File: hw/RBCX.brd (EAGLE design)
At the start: 100 x 100 mm, 463 parts, among them IC1 AMS1117-3.3, IC10 INA180A4, IC11 INA180A4, IC12 MPU-6050, IC13 STM32F103VCT6, IC2 DRV8833PWP, IC3 INA180A4, IC4 INA180A4, IC5 DRV8833PWP, IC6 INA180A4, IC7 INA180A4, IC8 INA180A4, IC9 INA180A4, P1 M1, P2 M2, P3 M3, P4 M4, Q1 NCE20P45Q, Q10 2N7002, Q2 NCE20P45Q, Q3 2N7002, Q4 2N7002, Q5 2N7002, Q6 2N7002, Q7 2N7002, Q8 2N7002, Q9 2N7002, X1 POWER_IN, X2 POWER_OUT, X3 52559-3092, X4 uUSB, Y1 5032/2P, Y2 3215_2P

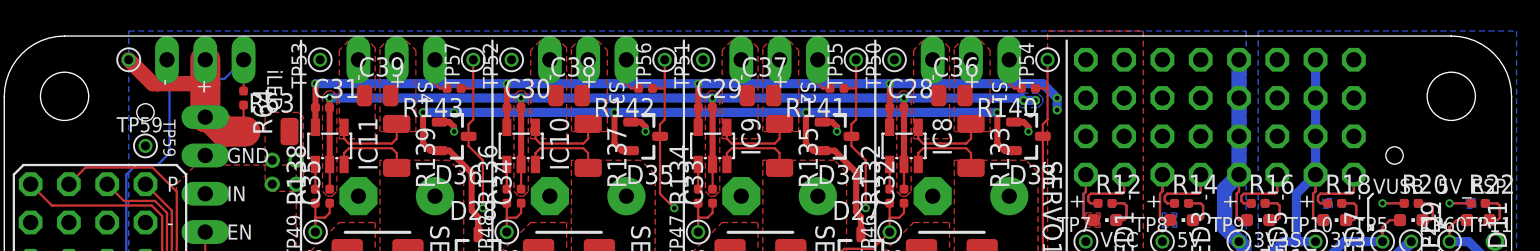
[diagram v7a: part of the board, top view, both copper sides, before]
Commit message: hw: add two small areas of unmasked GND plane for oscilloscope clip
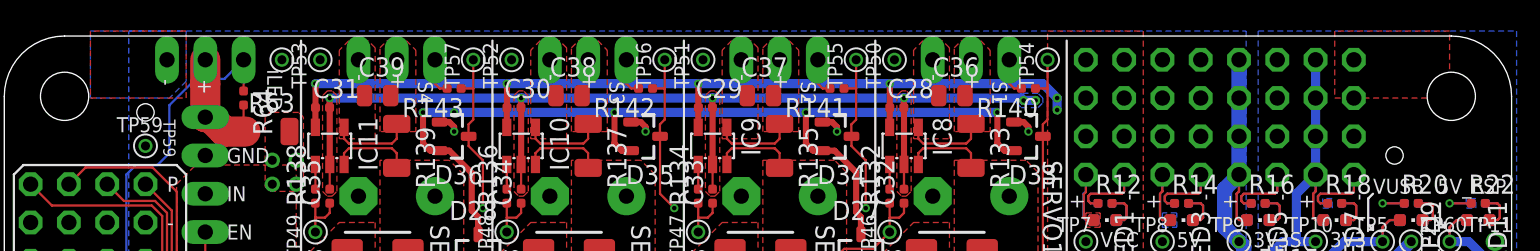
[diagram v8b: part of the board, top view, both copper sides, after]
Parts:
- moved TP15 10.2 mm to (18.4, 98.4)
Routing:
- net ILED-5V: track 98.2 -> 97.4 mm
- net ILED_PWR: track 14.4 -> 15.1 mm
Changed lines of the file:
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@@
 <layer number="13" name="Route13" color="21" fill="1" visible="no" active="no"/>
 <layer number="14" name="Route14" color="22" fill="1" visible="no" active="no"/>
-<layer number="15" name="Layer3-GND" color="23" fill="1" visible="yes" active="yes"/>
+<layer number="15" name="Layer3-GND" color="23" fill="1" visible="no" active="yes"/>
 <layer number="16" name="Bottom" color="1" fill="1" visible="yes" active="yes"/>
 <layer number="17" name="Pads" color="2" fill="1" visible="yes" active="yes"/>
@@
 <layer number="22" name="bPlace" color="7" fill="1" visible="yes" active="yes"/>
 <layer number="23" name="tOrigins" color="15" fill="1" visible="yes" active="yes"/>
-<layer number="24" name="bOrigins" color="15" fill="1" visible="no" active="yes"/>
+<layer number="24" name="bOrigins" color="15" fill="1" visible="yes" active="yes"/>
 <layer number="25" name="tNames" color="7" fill="1" visible="no" active="yes"/>
 <layer number="26" name="bNames" color="7" fill="1" visible="no" active="yes"/>
 <layer number="27" name="tValues" color="7" fill="1" visible="no" active="yes"/>
 <layer number="28" name="bValues" color="7" fill="1" visible="no" active="yes"/>
-<layer number="29" name="tStop" color="7" fill="3" visible="no" active="yes"/>
-<layer number="30" name="bStop" color="7" fill="6" visible="no" active="yes"/>
+<layer number="29" name="tStop" color="7" fill="3" visible="yes" active="yes"/>
+<layer number="30" name="bStop" color="7" fill="6" visible="yes" active="yes"/>
 <layer number="31" name="tCream" color="7" fill="4" visible="no" active="yes"/>
 <layer number="32" name="bCream" color="7" fill="5" visible="no" active="yes"/>
@@
 <layer number="38" name="bTest" color="7" fill="1" visible="no" active="yes"/>
 <layer number="39" name="tKeepout" color="4" fill="11" visible="yes" active="yes"/>
-<layer number="40" name="bKeepout" color="1" fill="11" visible="no" active="yes"/>
+<layer number="40" name="bKeepout" color="1" fill="11" visible="yes" active="yes"/>
 <layer number="41" name="tRestrict" color="4" fill="10" visible="yes" active="yes"/>
-<layer number="42" name="bRestrict" color="1" fill="10" visible="no" active="yes"/>
+<layer number="42" name="bRestrict" color="1" fill="10" visible="yes" active="yes"/>
 <layer number="43" name="vRestrict" color="2" fill="10" visible="yes" active="yes"/>
 <layer number="44" name="Drills" color="7" fill="1" visible="no" active="yes"/>
@@
 <layer number="99" name="SpiceOrder" color="7" fill="1" visible="no" active="no"/>
 <layer number="100" name="Muster" color="7" fill="1" visible="no" active="no"/>
-<layer number="101" name="tSilk" color="5" fill="1" visible="yes" active="yes"/>
-<layer number="102" name="bSilk" color="3" fill="1" visible="yes" active="yes"/>
+<layer number="101" name="tSilk" color="5" fill="1" visible="no" active="yes"/>
+<layer number="102" name="bSilk" color="3" fill="1" visible="no" active="yes"/>
 <layer number="113" name="ReferenceLS" color="7" fill="1" visible="no" active="no"/>
 <layer number="118" name="Rect_Pads" color="7" fill="1" visible="no" active="no"/>
@@
 <wire x1="75.08875" y1="24.4475" x2="75.08875" y2="15.08125" width="0.1524" layer="101"/>
 <wire x1="75.08875" y1="15.08125" x2="78.105" y2="12.065" width="0.1524" layer="101"/>
-<wire x1="92.075" y1="95.885" x2="92.075" y2="99.695" width="0.1524" layer="42"/>
 <wire x1="95.885" y1="92.075" x2="99.695" y2="92.075" width="0.1524" layer="42"/>
 <wire x1="92.075" y1="3.81" x2="92.075" y2="0.3175" width="0.1524" layer="42"/>
@@
 <wire x1="76.35875" y1="74.13625" x2="75.8825" y2="74.6125" width="0.2" layer="102"/>
 <wire x1="75.8825" y1="74.6125" x2="70.485" y2="74.6125" width="0.2" layer="102"/>
+<polygon width="0.2" layer="29">
+<vertex x="9.525" y="100.33"/>
+<vertex x="5.715" y="100.33"/>
+<vertex x="5.715" y="95.885"/>
+<vertex x="9.525" y="95.885"/>
+</polygon>
+<polygon width="0.2" layer="30">
+<vertex x="5.715" y="100.33"/>
+<vertex x="9.525" y="100.33"/>
+<vertex x="9.525" y="95.885"/>
+<vertex x="5.715" y="95.885"/>
+</polygon>
+<polygon width="0.2" layer="30">
+<vertex x="90.805" y="100.33"/>
+<vertex x="94.615" y="100.33"/>
+<vertex x="94.615" y="95.885"/>
+<vertex x="90.805" y="95.885"/>
+</polygon>
+<polygon width="0.2" layer="29">
+<vertex x="94.615" y="100.33"/>
+<vertex x="90.805" y="100.33"/>
+<vertex x="90.805" y="95.885"/>
+<vertex x="94.615" y="95.885"/>
+</polygon>
 </plain>
 <attributes>
@@
 <attribute name="VALUE" x="16.1925" y="91.1225" size="1.27" layer="27"/>
 </element>
-<element name="TP15" library="test_points" package="TP_06" value="" x="8.255" y="98.425" smashed="yes" rot="MR270">
-<attribute name="NAME" x="7.62" y="100.33" size="1" layer="26" font="vector" ratio="16" rot="MR270"/>
+<element name="TP15" library="test_points" package="TP_06" value="" x="18.415" y="98.425" smashed="yes" rot="MR270">
+<attribute name="NAME" x="17.78" y="100.33" size="1" layer="26" font="vector" ratio="16" rot="MR270"/>
 </element>
 <element name="R5" library="rcl_upravena" package="R0402" value="330R" x="24.765" y="52.705" smashed="yes" rot="R180">
@@
 <wire x1="76.35875" y1="84.29625" x2="76.35875" y2="74.8656875" width="0.6096" layer="2"/>
 <wire x1="76.35875" y1="72.4543125" x2="76.35875" y2="70.32625" width="0.6096" layer="2"/>
+<polygon width="0.2" layer="16">
+<vertex x="5.715" y="100.33"/>
+<vertex x="12.065" y="100.33"/>
+<vertex x="12.065" y="96.99625"/>
+<vertex x="10.95375" y="95.885"/>
+<vertex x="5.715" y="95.885"/>
+</polygon>
+<polygon width="0.2" layer="1">
+<vertex x="12.065" y="100.33"/>
+<vertex x="5.715" y="100.33"/>
+<vertex x="5.715" y="95.885"/>
+<vertex x="12.065" y="95.885"/>
+</polygon>
+<polygon width="0.2" layer="1">
+<vertex x="88.265" y="100.33"/>
+<vertex x="88.265" y="95.885"/>
+<vertex x="95.885" y="95.885"/>
+<vertex x="95.885" y="100.33"/>
+</polygon>
 </signal>
 <signal name="+3V3">
@@
 <wire x1="8.09625" y1="90.805" x2="8.73125" y2="91.44" width="0.1524" layer="16"/>
 <wire x1="10.16" y1="91.44" x2="10.95375" y2="92.23375" width="0.1524" layer="16"/>
-<wire x1="10.95375" y1="92.23375" x2="10.95375" y2="96.67875" width="0.1524" layer="16"/>
-<wire x1="10.95375" y1="96.67875" x2="11.43" y2="97.155" width="0.1524" layer="16"/>
-<wire x1="11.43" y1="97.155" x2="14.605" y2="97.155" width="0.1524" layer="16"/>
+<wire x1="10.95375" y1="92.23375" x2="10.95375" y2="95.40875" width="0.1524" layer="16"/>
+<wire x1="10.95375" y1="95.40875" x2="12.7" y2="97.155" width="0.1524" layer="16"/>
+<wire x1="12.7" y1="97.155" x2="14.605" y2="97.155" width="0.1524" layer="16"/>
 <wire x1="14.605" y1="97.155" x2="15.875" y2="98.425" width="0.1524" layer="16"/>
 <wire x1="8.73125" y1="91.44" x2="10.16" y2="91.44" width="0.1524" layer="16"/>
@@
 <wire x1="15.875" y1="95.42" x2="15.875" y2="93.79" width="0.1524" layer="1"/>
 <wire x1="15.875" y1="93.79" x2="16.0025" y2="93.6625" width="0.1524" layer="1"/>
-<wire x1="8.255" y1="98.425" x2="9.8395" y2="96.8405" width="1.016" layer="1"/>
-<wire x1="9.8395" y1="96.8405" x2="10.156575" y2="96.8405" width="1.016" layer="1"/>
-<wire x1="10.156575" y1="96.8405" x2="10.159575" y2="96.8375" width="1.016" layer="1"/>
-<wire x1="10.159575" y1="96.8375" x2="13.335" y2="96.8375" width="1.016" layer="1"/>
+<wire x1="18.415" y1="98.425" x2="16.8275" y2="96.8375" width="1.016" layer="2"/>
+<wire x1="16.8275" y1="96.8375" x2="14.9225" y2="96.8375" width="1.016" layer="2"/>
+<wire x1="14.9225" y1="96.8375" x2="13.335" y2="98.425" width="1.016" layer="2"/>
 </signal>
 <signal name="BUTTON-ON-LV">
